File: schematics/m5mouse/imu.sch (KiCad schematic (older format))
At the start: 4 parts, among them U4 MPU9250_9255

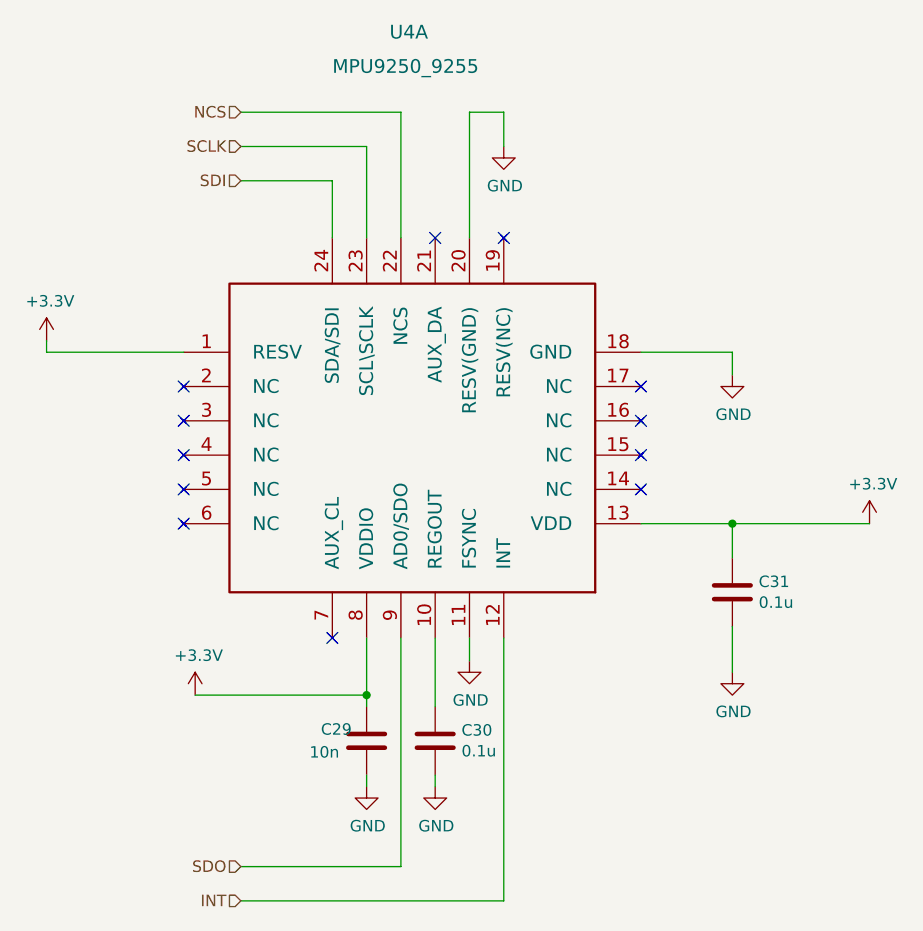
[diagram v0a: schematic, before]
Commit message: Fix schematics and patterns
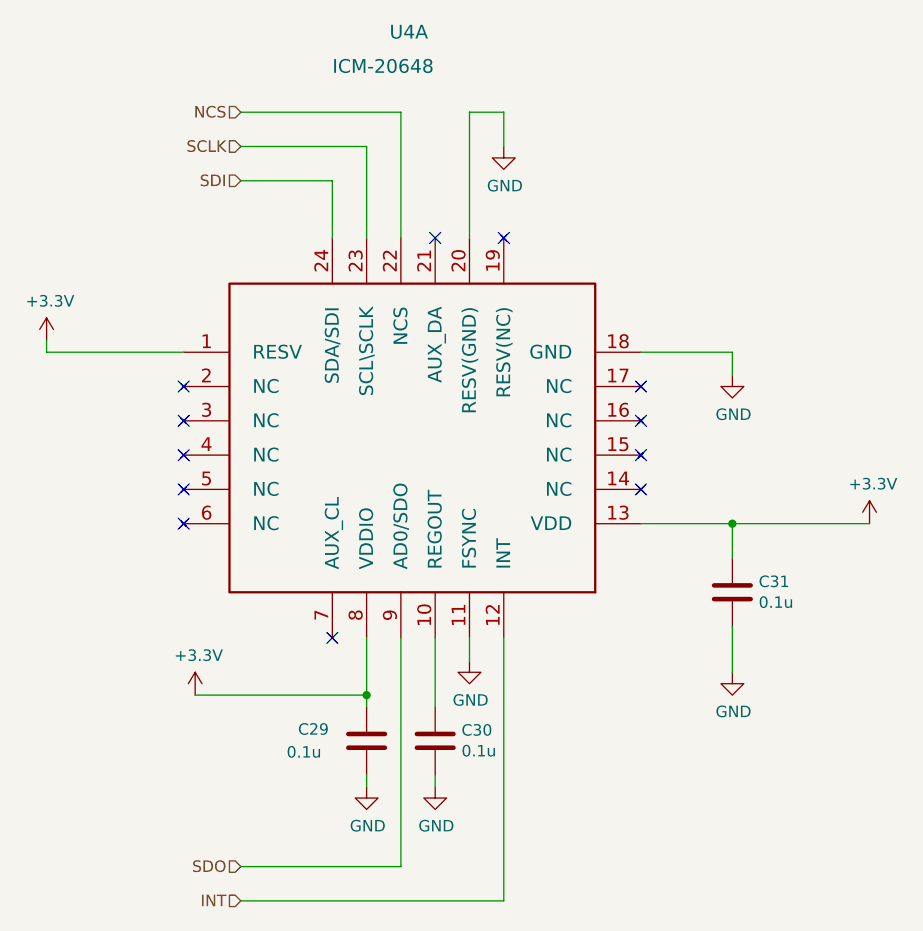
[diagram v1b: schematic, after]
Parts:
- C29: value 10n -> 0.1u
- U4: value MPU9250_9255 -> ICM-20648; Manf# (none) -> ICM-20948; URL (none) -> https://www.digikey.jp/product-detail/ja/tdk-invensense/ICM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
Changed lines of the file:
@@
 P 5900 3750
 F 0 "U4" H 5800 5550 60  0000 L CNN
-F 1 "MPU9250_9255" H 5550 5400 60  0000 L CNN
+F 1 "ICM-20648" H 5550 5400 60  0000 L CNN
 F 2 "Package_DFN_QFN:QFN-24-1EP_3x3mm_P0.4mm_EP1.75x1.6mm" H 5950 3750 60  0001 C CNN
 F 3 "" H 5950 3750 60  0000 C CNN
+F 4 "https://www.digikey.jp/product-detail/ja/tdk-invensense/ICM-20948/1428-1123-1-ND/7062698" H 5900 3750 50  0001 C CNN "URL"
+F 5 "ICM-20948" H 5900 3750 50  0001 C CNN "Manf#"
 	1    5900 3750
 	1    0    0    -1
@@
 U 1 1 5F49C7B2
 P 5700 5050
-F 0 "C29" H 5500 5100 50  0000 L CNN
-F 1 "10n" H 5450 5000 50  0000 L CNN
+F 0 "C29" H 5400 5100 50  0000 L CNN
+F 1 "0.1u" H 5350 5000 50  0000 L CNN
 F 2 "Capacitor_SMD:C_0402_1005Metric" H 5738 4900 50  0001 C CNN
 F 3 "~" H 5700 5050 50  0001 C CNN

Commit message: Fix pattern
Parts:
- U4: Manf# ICM-20948 -> ICM-20648; URL https://www.digikey.jp/product-detail/ja/tdk-invensense/ICM-20948/1428-1123-1-ND/7062698 -> https://www.digikey.jp/product-detail/ja/tdk-invensense/ICM-20648/1428-1061-1-ND/5872876
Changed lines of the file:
@@
 F 2 "Package_DFN_QFN:QFN-24-1EP_3x3mm_P0.4mm_EP1.75x1.6mm" H 5950 3750 60  0001 C CNN
 F 3 "" H 5950 3750 60  0000 C CNN
-F 4 "https://www.digikey.jp/product-detail/ja/tdk-invensense/ICM-20948/1428-1123-1-ND/7062698" H 5900 3750 50  0001 C CNN "URL"
-F 5 "ICM-20948" H 5900 3750 50  0001 C CNN "Manf#"
+F 4 "https://www.digikey.jp/product-detail/ja/tdk-invensense/ICM-20648/1428-1061-1-ND/5872876" H 5900 3750 50  0001 C CNN "URL"
+F 5 "ICM-20648" H 5900 3750 50  0001 C CNN "Manf#"
 	1    5900 3750
 	1    0    0    -1

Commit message: Fix schematics
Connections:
- net +3V3: no longer U4.1 (RESV)
- no-connect marks 12 -> 13
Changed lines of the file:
@@
 Wire Wire Line
 	5700 2450 5700 2850
-$Comp
-L power:+3.3V #PWR029
-U 1 1 5F4A8D10
-P 4300 3300
-F 0 "#PWR029" H 4300 3150 50  0001 C CNN
-F 1 "+3.3V" H 4315 3473 50  0000 C CNN
-F 2 "" H 4300 3300 50  0001 C CNN
-F 3 "" H 4300 3300 50  0001 C CNN
-	1    4300 3300
-	1    0    0    -1
-$EndComp
-Wire Wire Line
-	4300 3300 4300 3350
-Wire Wire Line
-	4300 3350 4900 3350
 NoConn ~ 5550 4600
 $Comp
@@
 Wire Wire Line
 	5150 5750 6300 5750
+NoConn ~ 4900 3350
 $EndSCHEMATC
